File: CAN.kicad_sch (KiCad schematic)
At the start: 10 parts, among them J3 Conn_01x03, U4 MCP2551-I/SN, U5 LTV-355T

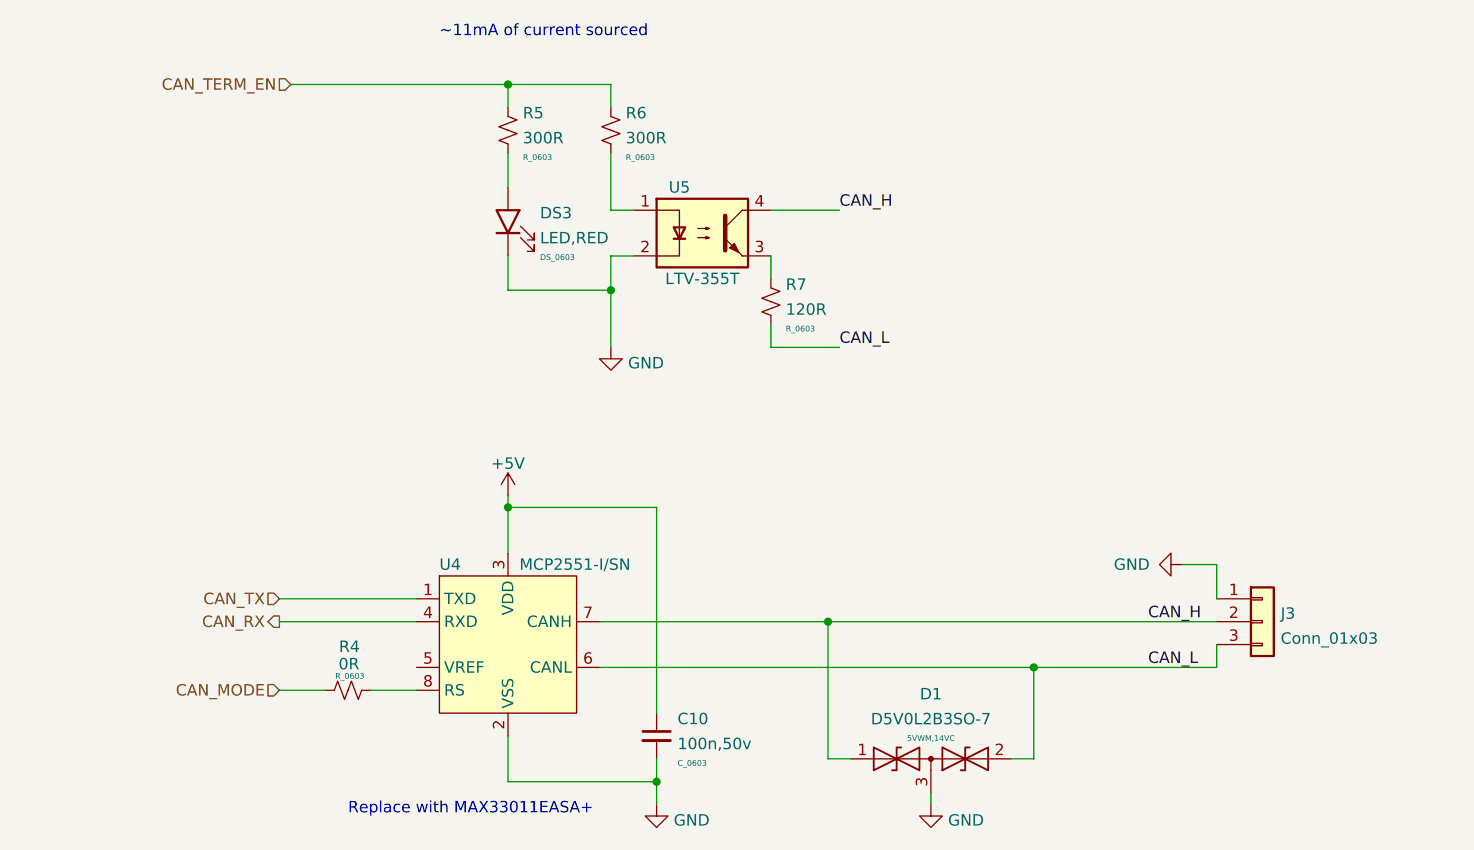
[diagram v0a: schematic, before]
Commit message: Added connection for fault pin. Reversed CAN connector.
Updated some footprints
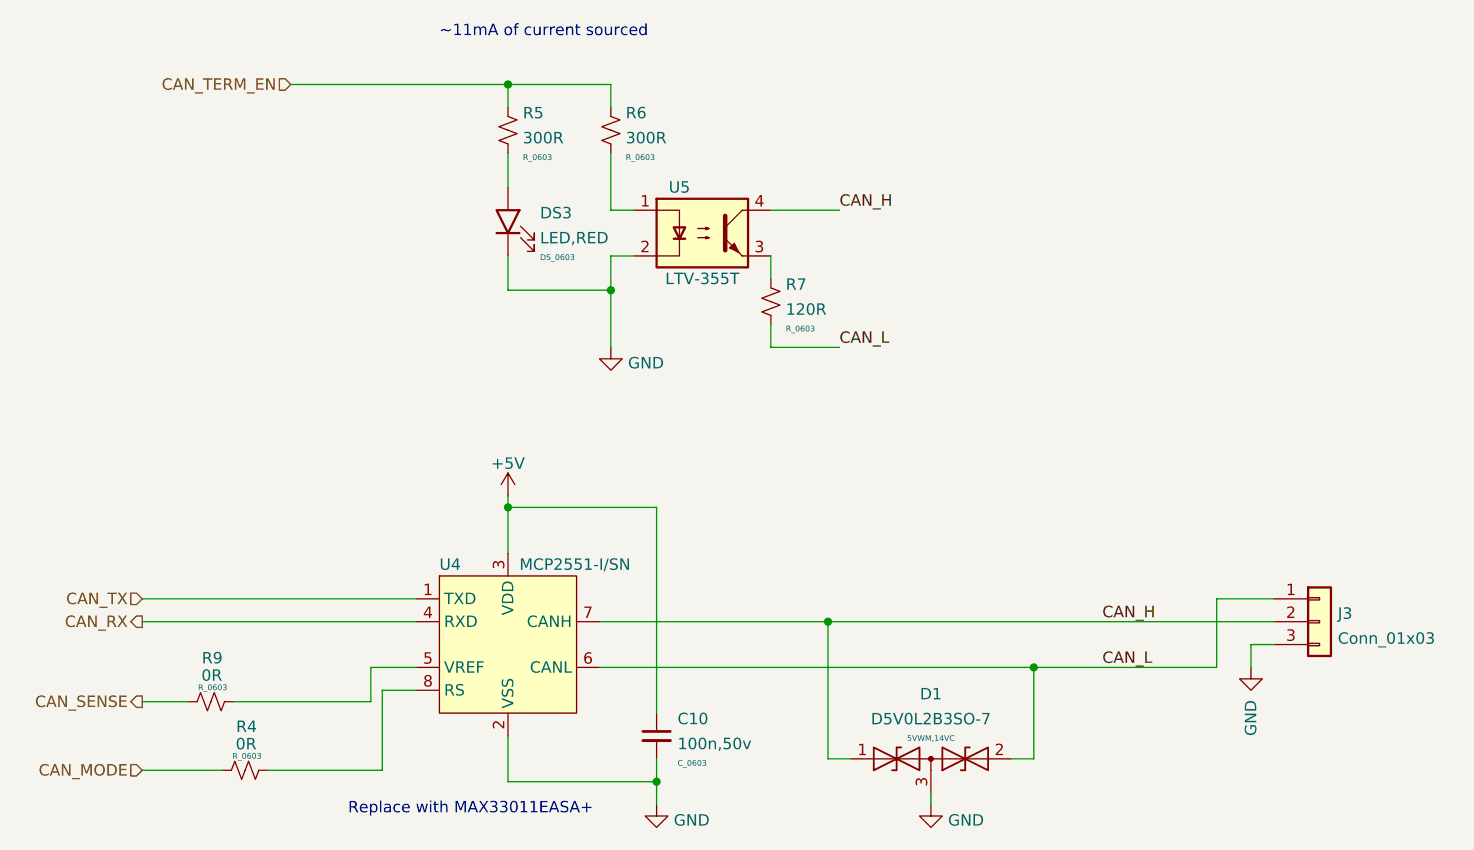
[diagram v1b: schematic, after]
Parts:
- added R9: 0R, R_Resistor:R_0603, symbol R_Resistor:R_0603
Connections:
- net CAN_L: now also J3.1 (Pin_1); no longer J3.3 (Pin_3)
- net GND: now also J3.3 (Pin_3); no longer J3.1 (Pin_1)
- net at U4.5 (VREF): now also R9.2
- new net CAN_SENSE: R9.1
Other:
- moved on the sheet: R4
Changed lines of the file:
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@@
+    (stroke (width 0) (type default) (color 0 0 0 0))
+  )
+  (wire (pts (xy 59.69 121.92) (xy 64.77 121.92))
     (stroke (width 0) (type default) (color 0 0 0 0))
   )
@@
     (stroke (width 0) (type default) (color 0 0 0 0))
   )
+  (wire (pts (xy 85.09 118.11) (xy 85.09 121.92))
+    (stroke (width 0) (type default) (color 0 0 0 0))
+  )
   (wire (pts (xy 135.89 128.27) (xy 135.89 113.03))
     (stroke (width 0) (type default) (color 0 0 0 0))
@@
     (stroke (width 0) (type default) (color 0 0 0 0))
   )
+  (wire (pts (xy 179.07 110.49) (xy 185.42 110.49))
+    (stroke (width 0) (type default) (color 0 0 0 0))
+  )
   (wire (pts (xy 100.33 53.34) (xy 100.33 55.88))
     (stroke (width 0) (type default) (color 0 0 0 0))
@@
     (stroke (width 0) (type default) (color 0 0 0 0))
   )
+  (wire (pts (xy 73.66 129.54) (xy 86.36 129.54))
+    (stroke (width 0) (type default) (color 0 0 0 0))
+  )
   (wire (pts (xy 100.33 99.06) (xy 100.33 100.33))
     (stroke (width 0) (type default) (color 0 0 0 0))
@@
     (stroke (width 0) (type default) (color 0 0 0 0))
   )
-  (wire (pts (xy 74.93 110.49) (xy 90.17 110.49))
+  (wire (pts (xy 86.36 129.54) (xy 86.36 120.65))
+    (stroke (width 0) (type default) (color 0 0 0 0))
+  )
+  (wire (pts (xy 85.09 121.92) (xy 69.85 121.92))
+    (stroke (width 0) (type default) (color 0 0 0 0))
+  )
+  (wire (pts (xy 59.69 110.49) (xy 90.17 110.49))
     (stroke (width 0) (type default) (color 0 0 0 0))
   )
@@
     (stroke (width 0) (type default) (color 0 0 0 0))
   )
-  (wire (pts (xy 175.26 106.68) (xy 179.07 106.68))
-    (stroke (width 0) (type default) (color 0 0 0 0))
-  )
   (wire (pts (xy 129.54 82.55) (xy 129.54 80.01))
     (stroke (width 0) (type default) (color 0 0 0 0))
@@
     (stroke (width 0) (type default) (color 0 0 0 0))
   )
-  (wire (pts (xy 179.07 106.68) (xy 179.07 110.49))
-    (stroke (width 0) (type default) (color 0 0 0 0))
-  )
-  (wire (pts (xy 74.93 113.03) (xy 90.17 113.03))
-    (stroke (width 0) (type default) (color 0 0 0 0))
-  )
-  (wire (pts (xy 135.89 113.03) (xy 179.07 113.03))
-    (stroke (width 0) (type default) (color 0 0 0 0))
-  )
-  (wire (pts (xy 179.07 115.57) (xy 179.07 118.11))
+  (wire (pts (xy 182.88 118.11) (xy 182.88 115.57))
+    (stroke (width 0) (type default) (color 0 0 0 0))
+  )
+  (wire (pts (xy 59.69 113.03) (xy 90.17 113.03))
+    (stroke (width 0) (type default) (color 0 0 0 0))
+  )
+  (wire (pts (xy 135.89 113.03) (xy 185.42 113.03))
+    (stroke (width 0) (type default) (color 0 0 0 0))
+  )
+  (wire (pts (xy 179.07 110.49) (xy 179.07 118.11))
     (stroke (width 0) (type default) (color 0 0 0 0))
   )
@@
     (stroke (width 0) (type default) (color 0 0 0 0))
   )
+  (wire (pts (xy 86.36 120.65) (xy 90.17 120.65))
+    (stroke (width 0) (type default) (color 0 0 0 0))
+  )
+  (wire (pts (xy 182.88 115.57) (xy 185.42 115.57))
+    (stroke (width 0) (type default) (color 0 0 0 0))
+  )
   (wire (pts (xy 116.84 130.81) (xy 116.84 128.27))
     (stroke (width 0) (type default) (color 0 0 0 0))
@@
     (stroke (width 0) (type default) (color 0 0 0 0))
   )
-  (wire (pts (xy 74.93 120.65) (xy 80.01 120.65))
+  (wire (pts (xy 59.69 129.54) (xy 68.58 129.54))
+    (stroke (width 0) (type default) (color 0 0 0 0))
+  )
+  (wire (pts (xy 90.17 118.11) (xy 85.09 118.11))
     (stroke (width 0) (type default) (color 0 0 0 0))
   )
@@
     (stroke (width 0) (type default) (color 0 0 0 0))
   )
-  (wire (pts (xy 85.09 120.65) (xy 90.17 120.65))
-    (stroke (width 0) (type default) (color 0 0 0 0))
-  )
   (wire (pts (xy 100.33 72.39) (xy 100.33 76.2))
     (stroke (width 0) (type default) (color 0 0 0 0))
@@
     (effects (font (size 1.27 1.27)) (justify left bottom))
   )
-  (label "CAN_L" (at 171.45 118.11 0)
-    (effects (font (size 1.27 1.27)) (justify left bottom))
-  )
-  (label "CAN_H" (at 171.45 113.03 0)
+  (label "CAN_L" (at 166.37 118.11 0)
+    (effects (font (size 1.27 1.27)) (justify left bottom))
+  )
+  (label "CAN_H" (at 166.37 113.03 0)
     (effects (font (size 1.27 1.27)) (justify left bottom))
   )
@@
     (effects (font (size 1.27 1.27)) (justify left bottom))
   )
-  (hierarchical_label "CAN_TX" (shape input) (at 74.93 110.49 180)
-    (effects (font (size 1.27 1.27)) (justify right))
-  )
-  (hierarchical_label "CAN_RX" (shape output) (at 74.93 113.03 180)
+  (hierarchical_label "CAN_TX" (shape input) (at 59.69 110.49 180)
+    (effects (font (size 1.27 1.27)) (justify right))
+  )
+  (hierarchical_label "CAN_RX" (shape output) (at 59.69 113.03 180)
     (effects (font (size 1.27 1.27)) (justify right))
   )
@@
     (effects (font (size 1.27 1.27)) (justify right))
   )
-  (hierarchical_label "CAN_MODE" (shape input) (at 74.93 120.65 180)
+  (hierarchical_label "CAN_SENSE" (shape output) (at 59.69 121.92 180)
+    (effects (font (size 1.27 1.27)) (justify right))
+  )
+  (hierarchical_label "CAN_MODE" (shape input) (at 59.69 129.54 180)
     (effects (font (size 1.27 1.27)) (justify right))
   )
@@
     (pin "2")
   )
-  (symbol (lib_id "Connector_Generic:Conn_01x03") (at 184.15 113.03 0) (unit 1)
-    (in_bom yes) (on_board yes) (fields_autoplaced)
-    (property "Reference" "J3" (id 0) (at 186.182 112.1215 0)
-      (effects (font (size 1.27 1.27)) (justify left))
-    )
-    (property "Value" "Conn_01x03" (id 1) (at 186.182 114.8966 0)
-      (effects (font (size 1.27 1.27)) (justify left))
-    )
-    (property "Footprint" "Connector_Phoenix_MSTB:PhoenixContact_MSTBA_2,5_3-G-5,08_1x03_P5.08mm_Horizontal" (id 2) (at 184.15 113.03 0)
-      (effects (font (size 1.27 1.27)) hide)
-    )
-    (property "Datasheet" "~" (id 3) (at 184.15 113.03 0)
-      (effects (font (size 1.27 1.27)) hide)
-    )
-    (pin "1")
-    (pin "2")
-    (pin "3")
-  )
-  (symbol (lib_id "power:GND") (at 175.26 106.68 270) (unit 1)
+  (symbol (lib_id "power:GND") (at 182.88 118.11 0) (unit 1)
     (in_bom yes) (on_board yes)
-    (property "Reference" "#PWR0101" (id 0) (at 168.91 106.68 0)
-      (effects (font (size 1.27 1.27)) hide)
-    )
-    (property "Value" "GND" (id 1) (at 167.64 106.68 90)
-      (effects (font (size 1.27 1.27)) (justify left))
-    )
-    (property "Footprint" "" (id 2) (at 175.26 106.68 0)
-      (effects (font (size 1.27 1.27)) hide)
-    )
-    (property "Datasheet" "" (id 3) (at 175.26 106.68 0)
+    (property "Reference" "#PWR0101" (id 0) (at 182.88 124.46 0)
+      (effects (font (size 1.27 1.27)) hide)
+    )
+    (property "Value" "GND" (id 1) (at 182.88 125.73 90)
+      (effects (font (size 1.27 1.27)) (justify left))
+    )
+    (property "Footprint" "" (id 2) (at 182.88 118.11 0)
+      (effects (font (size 1.27 1.27)) hide)
+    )
+    (property "Datasheet" "" (id 3) (at 182.88 118.11 0)
       (effects (font (size 1.27 1.27)) hide)
     )
@@
     (pin "3")
   )
-  (symbol (lib_id "R_Resistor:R_0603") (at 82.55 120.65 90) (unit 1)
+  (symbol (lib_id "R_Resistor:R_0603") (at 71.12 129.54 90) (unit 1)
     (in_bom yes) (on_board yes)
-    (property "Reference" "R4" (id 0) (at 83.8669 115.8072 90)
-      (effects (font (size 1.27 1.27)) (justify left))
-    )
-    (property "Value" "0R" (id 1) (at 83.8199 117.734 90)
-      (effects (font (size 1.27 1.27)) (justify left))
-    )
-    (property "Footprint" "R_Resistor:R_0603" (id 2) (at 82.55 123.19 90)
-      (effects (font (size 1.27 1.27)) hide)
-    )
-    (property "Datasheet" "" (id 3) (at 86.36 123.19 0)
-      (effects (font (size 1.27 1.27)) hide)
-    )
-    (property "Size" "R_0603" (id 4) (at 84.3839 119.0734 90)
+    (property "Reference" "R4" (id 0) (at 72.4369 124.6972 90)
+      (effects (font (size 1.27 1.27)) (justify left))
+    )
+    (property "Value" "0R" (id 1) (at 72.3899 126.624 90)
+      (effects (font (size 1.27 1.27)) (justify left))
+    )
+    (property "Footprint" "R_Resistor:R_0603" (id 2) (at 71.12 132.08 90)
+      (effects (font (size 1.27 1.27)) hide)
+    )
+    (property "Datasheet" "" (id 3) (at 74.93 132.08 0)
+      (effects (font (size 1.27 1.27)) hide)
+    )
+    (property "Size" "R_0603" (id 4) (at 72.9539 127.9634 90)
       (effects (font (size 0.635 0.635)) (justify left))
     )
@@
     (pin "8")
   )
+  (symbol (lib_id "Connector_Generic:Conn_01x03") (at 190.5 113.03 0) (unit 1)
+    (in_bom yes) (on_board yes) (fields_autoplaced)
+    (property "Reference" "J3" (id 0) (at 192.532 112.1215 0)
+      (effects (font (size 1.27 1.27)) (justify left))
+    )
+    (property "Value" "Conn_01x03" (id 1) (at 192.532 114.8966 0)
+      (effects (font (size 1.27 1.27)) (justify left))
+    )
+    (property "Footprint" "Connector_Phoenix_MSTB:PhoenixContact_MSTBA_2,5_3-G-5,08_1x03_P5.08mm_Horizontal" (id 2) (at 190.5 113.03 0)
+      (effects (font (size 1.27 1.27)) hide)
+    )
+    (property "Datasheet" "~" (id 3) (at 190.5 113.03 0)
+      (effects (font (size 1.27 1.27)) hide)
+    )
+    (pin "1")
+    (pin "2")
+    (pin "3")
+  )
+  (symbol (lib_id "R_Resistor:R_0603") (at 67.31 121.92 90) (unit 1)
+    (in_bom yes) (on_board yes)
+    (property "Reference" "R9" (id 0) (at 68.6269 117.0772 90)
+      (effects (font (size 1.27 1.27)) (justify left))
+    )
+    (property "Value" "0R" (id 1) (at 68.5799 119.004 90)
+      (effects (font (size 1.27 1.27)) (justify left))
+    )
+    (property "Footprint" "R_Resistor:R_0603" (id 2) (at 67.31 124.46 90)
+      (effects (font (size 1.27 1.27)) hide)
+    )
+    (property "Datasheet" "" (id 3) (at 71.12 124.46 0)
+      (effects (font (size 1.27 1.27)) hide)
+    )
+    (property "Size" "R_0603" (id 4) (at 69.1439 120.3434 90)
+      (effects (font (size 0.635 0.635)) (justify left))
+    )
+    (pin "1")
+    (pin "2")
+  )
   (symbol (lib_id "U_Optos:LTV-355T") (at 121.92 69.85 0) (unit 1)

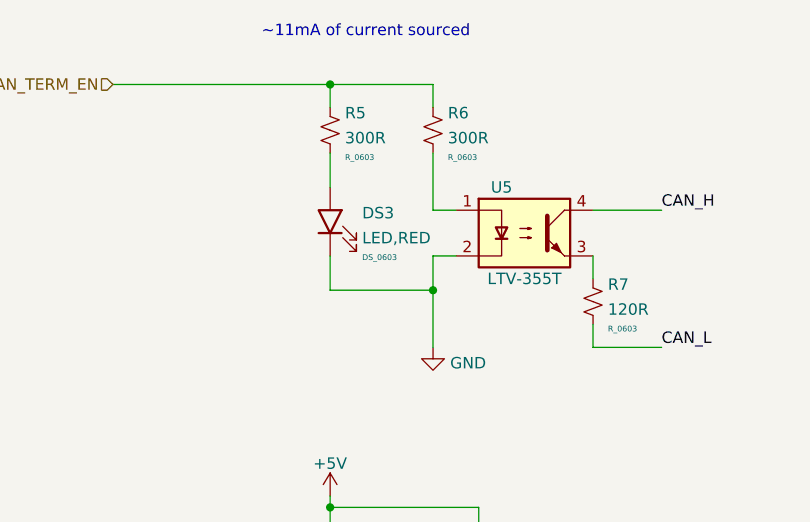
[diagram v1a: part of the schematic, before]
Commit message: Correct LED colors
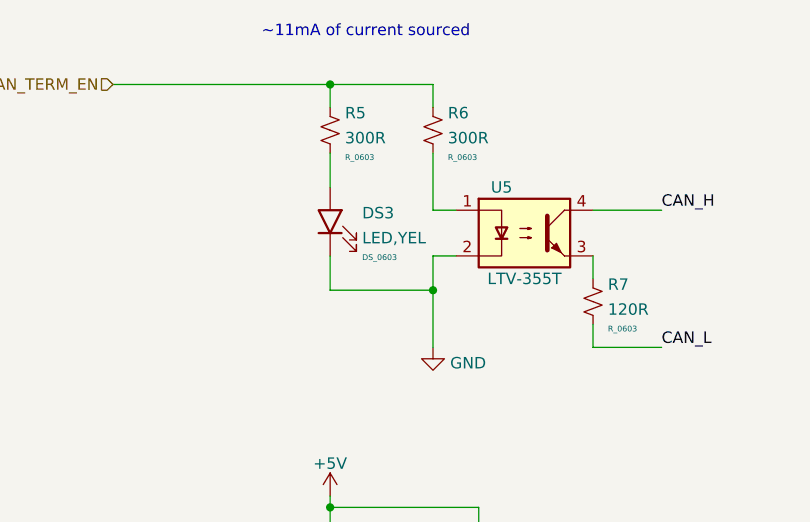
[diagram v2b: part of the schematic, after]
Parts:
- DS3: value LED,RED -> LED,YEL
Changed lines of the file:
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@@
       (effects (font (size 1.27 1.27)) (justify right))
     )
-    (property "Value" "LED,RED" (id 1) (at 103.886 70.4023 90)
+    (property "Value" "LED,YEL" (id 1) (at 103.886 70.4023 90)
       (effects (font (size 1.27 1.27)) (justify right))
     )
